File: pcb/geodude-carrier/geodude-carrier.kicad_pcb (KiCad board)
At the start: 2 copper layers, 154.9 x 152.3 mm, 44 parts, among them J1 12V, J2 12V, J3 GND, J30 SCL, J31 SCL, J32 SDA, J33 SDA, J34 3V3, J35 3V3, J36 5V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

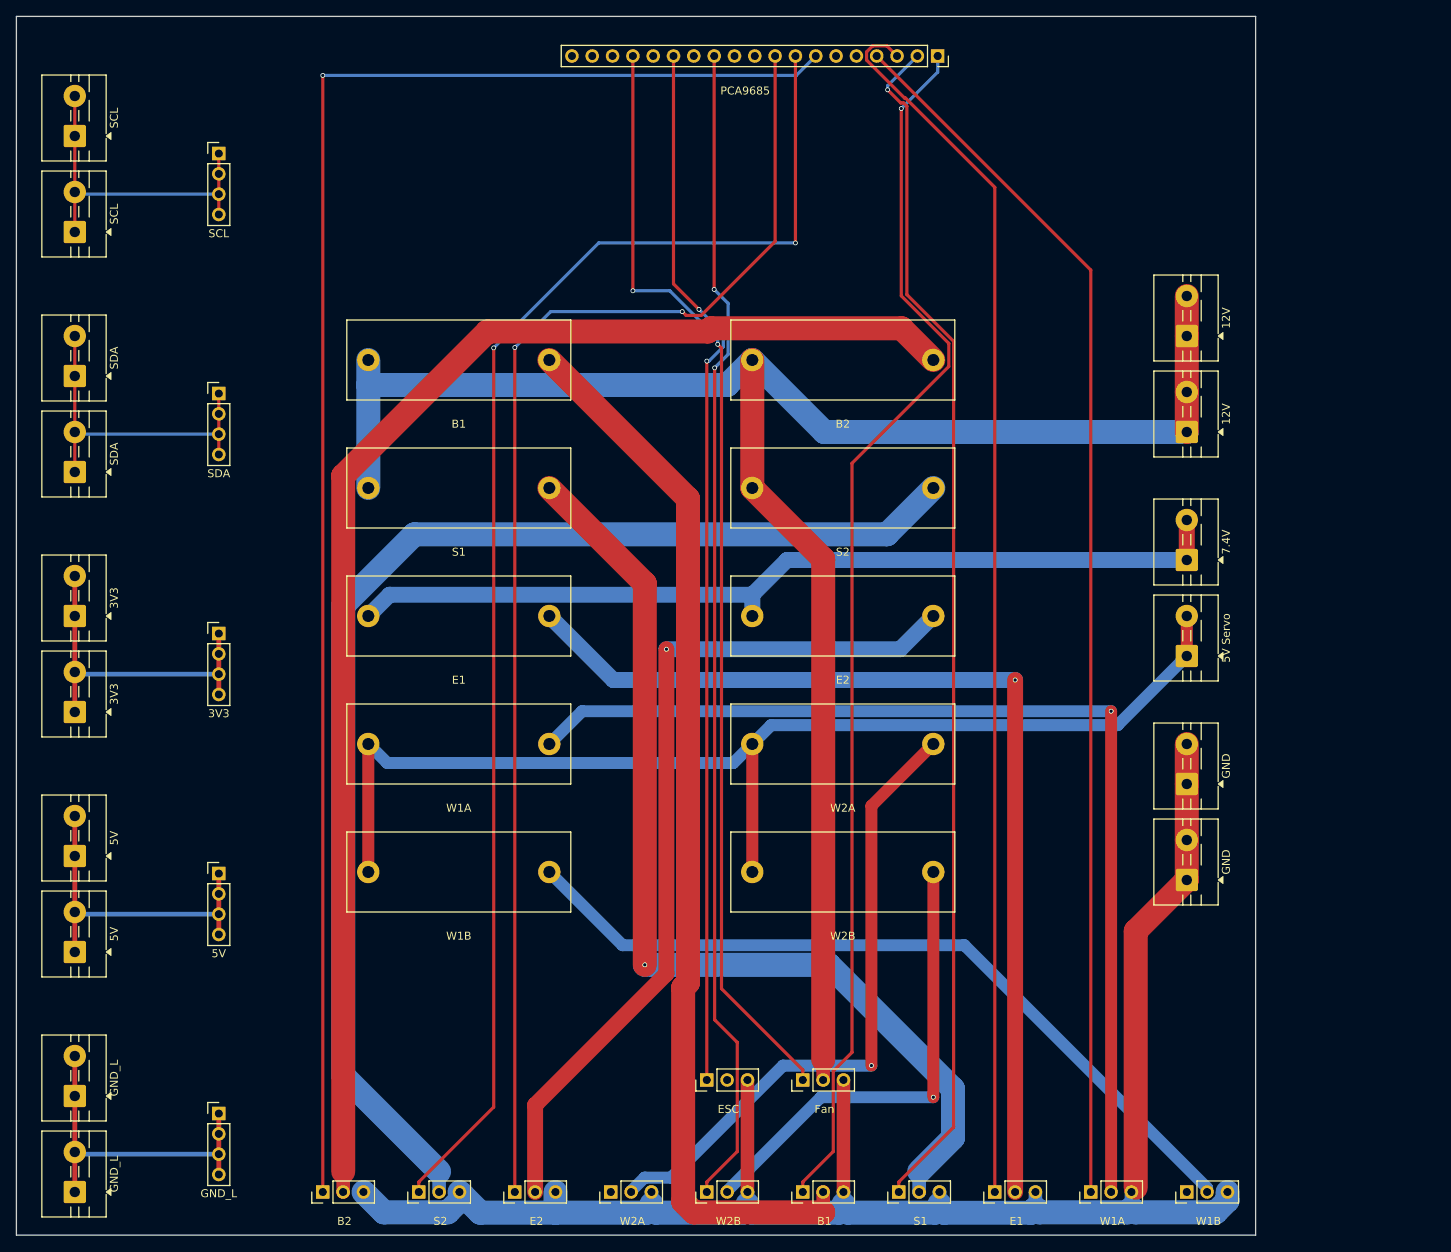
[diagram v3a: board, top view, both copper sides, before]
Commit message: Fully routed: fuses swapped to match servo sides, 0 unconnected, JLCPCB vias
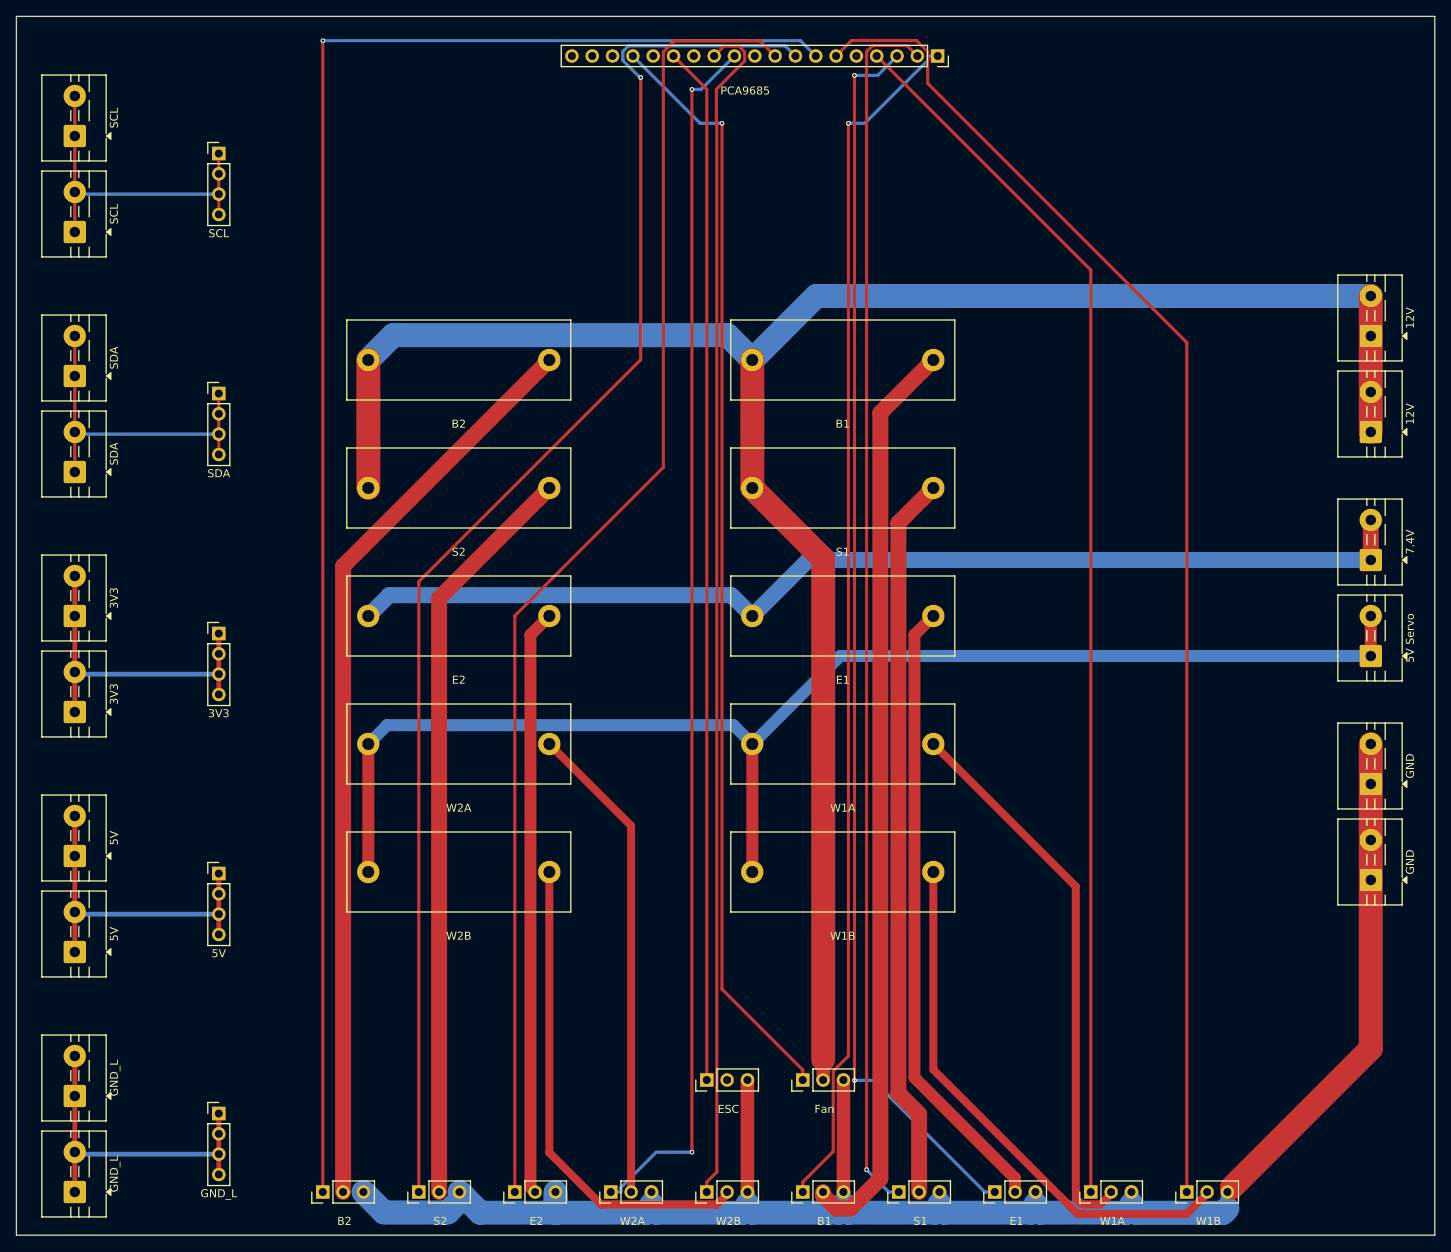
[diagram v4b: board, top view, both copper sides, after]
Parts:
- moved F1 48.0 mm to (106.0, 48.0)
- moved F10 48.0 mm to (58.0, 112.0)
- moved F2 48.0 mm to (106.0, 64.0)
- moved F3 48.0 mm to (106.0, 80.0)
- moved F4 48.0 mm to (106.0, 96.0)
- moved F5 48.0 mm to (106.0, 112.0)
- moved F6 48.0 mm to (58.0, 48.0)
- moved F7 48.0 mm to (58.0, 64.0)
- moved F8 48.0 mm to (58.0, 80.0)
- moved F9 48.0 mm to (58.0, 96.0)
- moved J1 23.0 mm to (172.0, 45.0)
- moved J2 23.0 mm to (172.0, 57.0)
- moved J3 23.0 mm to (172.0, 101.0)
- moved J4 23.0 mm to (172.0, 113.0)
- moved J5 23.0 mm to (172.0, 73.0)
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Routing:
- net PWM_CH4: track 0.00 -> 168.8 mm
- net PWM_CH8: track 0.00 -> 152.4 mm, vias 0 -> 2
- net SV7_PWR: track 158.1 -> 93.7 mm
- net SV4_PWR: track 132.0 -> 69.7 mm, vias 1 -> 0
- net SV6_PWR: track 172.6 -> 114.7 mm
- net SV3_PWR: track 125.5 -> 78.2 mm, vias 1 -> 0
- net SV8_PWR: track 109.7 -> 73.2 mm, vias 1 -> 0
- net SV2_PWR: track 124.1 -> 90.9 mm, vias 1 -> 0
- net SV5_PWR: track 99.1 -> 67.7 mm
- net +12V: track 234.0 -> 257.9 mm
- net +5V_SERVO: track 145.8 -> 168.8 mm
- net +7V4: track 112.9 -> 135.4 mm
- net SV9_PWR: track 80.1 -> 60.2 mm, vias 1 -> 0
- net SV1_PWR: track 133.3 -> 114.9 mm
- net GND: track 217.6 -> 222.8 mm
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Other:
- board size 154.9 x 152.3 mm -> 177.3 x 152.3 mm

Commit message: Production ready: copper pours (GND B.Cu, 12V F.Cu), Gerbers exported, 0 DRC errors
- GND copper pour on back layer (full board)
- +12V copper pour on front layer (right half, power area)
- Gerbers: F.Cu, B.Cu, F.Silk, B.Silk, F.Mask, B.Mask, Edge.Cuts, drill
- DRC: 0 violations, 0 unconnected (3 silk warnings)
- Vias: 0.3mm/0.4mm (JLCPCB free tier)
- Trace widths verified against IPC-2221 at 2oz copper
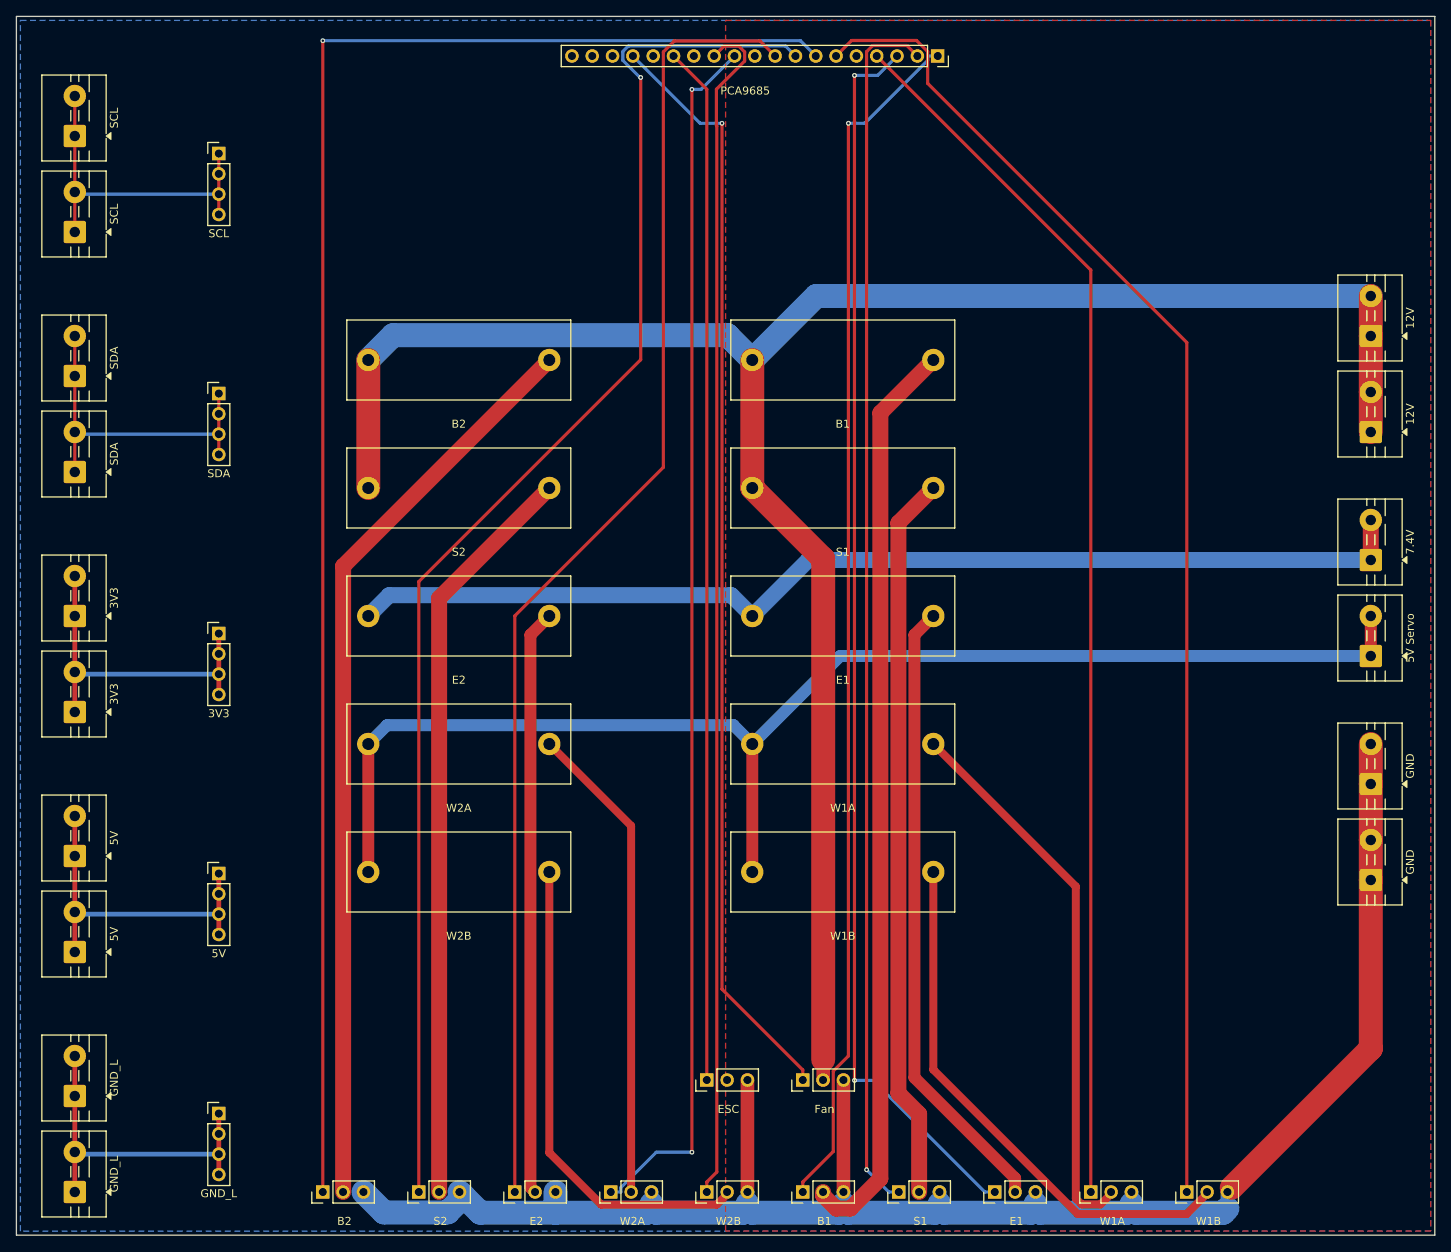
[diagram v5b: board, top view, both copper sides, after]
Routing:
- added copper zone on F.Cu, net +12V
- added copper zone on B.Cu, net GND
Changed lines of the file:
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@@
 		(net "PWM_CH12")
+	)
+	(zone
+		(net "+12V")
+		(layer "F.Cu")
+		(hatch edge 0.5)
+		(connect_pads
+			(clearance 0.5)
+		)
+		(min_thickness 0.3)
+		(fill yes
+			(thermal_gap 0.5)
+			(thermal_bridge_width 0.8)
+			(island_removal_mode 0)
+		)
+		(polygon
+			(pts
+				(xy 91.35 5.55) (xy 179.5 5.55) (xy 179.5 156.893796) (xy 91.35 156.893796)
+			)
+		)
+	)
+	(zone
+		(net "GND")
+		(layer "B.Cu")
+		(hatch edge 0.5)
+		(connect_pads
+			(clearance 0.5)
+		)
+		(min_thickness 0.3)
+		(fill yes
+			(thermal_gap 0.5)
+			(thermal_bridge_width 0.5)
+			(island_removal_mode 0)
+		)
+		(polygon
+			(pts
+				(xy 3.2 5.55) (xy 179.5 5.55) (xy 179.5 156.893796) (xy 3.2 156.893796)
+			)
+		)
 	)
 	(embedded_fonts no)

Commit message: Manual placement adjustments
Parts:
- moved J1 20.4 mm to (151.6, 46.2)
- moved J2 20.4 mm to (151.6, 58.2)
- moved J3 20.4 mm to (151.6, 102.2)
- moved J4 20.4 mm to (151.6, 114.2)
- moved J5 20.4 mm to (151.6, 74.2)
- moved J6 20.4 mm to (151.6, 86.2)
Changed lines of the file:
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@@
 	(footprint "TerminalBlock_MaiXu_MX126-5.0-02P_1x02_P5.00mm"
 		(layer "F.Cu")
-		(at 172 113 90)
+		(at 151.6 114.2 90)
 		(descr "terminal block MaiXu MX126-5.0-02P, 2 pins, pitch 5mm, size 10.5x7.8mm, drill diameter 1.3mm, pad diameter 2.8mm, https://www.lcsc.com/datasheet/lcsc_datasheet_2309150913_MAX-MX126-5-0-03P-GN01-Cu-S-A_C5188435.pdf")
 		(tags "THT terminal block MaiXu MX126-5.0-02P pitch 5mm size 10.5x7.8mm drill 1.3mm pad 2.8mm")
@@
 	(footprint "TerminalBlock_MaiXu_MX126-5.0-02P_1x02_P5.00mm"
 		(layer "F.Cu")
-		(at 172 57 90)
+		(at 151.6 58.2 90)
 		(descr "terminal block MaiXu MX126-5.0-02P, 2 pins, pitch 5mm, size 10.5x7.8mm, drill diameter 1.3mm, pad diameter 2.8mm, https://www.lcsc.com/datasheet/lcsc_datasheet_2309150913_MAX-MX126-5-0-03P-GN01-Cu-S-A_C5188435.pdf")
 		(tags "THT terminal block MaiXu MX126-5.0-02P pitch 5mm size 10.5x7.8mm drill 1.3mm pad 2.8mm")
@@
 	(footprint "TerminalBlock_MaiXu_MX126-5.0-02P_1x02_P5.00mm"
 		(layer "F.Cu")
-		(at 172 45 90)
+		(at 151.6 46.2 90)
 		(descr "terminal block MaiXu MX126-5.0-02P, 2 pins, pitch 5mm, size 10.5x7.8mm, drill diameter 1.3mm, pad diameter 2.8mm, https://www.lcsc.com/datasheet/lcsc_datasheet_2309150913_MAX-MX126-5-0-03P-GN01-Cu-S-A_C5188435.pdf")
 		(tags "THT terminal block MaiXu MX126-5.0-02P pitch 5mm size 10.5x7.8mm drill 1.3mm pad 2.8mm")
@@
 	(footprint "TerminalBlock_MaiXu_MX126-5.0-02P_1x02_P5.00mm"
 		(layer "F.Cu")
-		(at 172 85 90)
+		(at 151.6 86.2 90)
 		(descr "terminal block MaiXu MX126-5.0-02P, 2 pins, pitch 5mm, size 10.5x7.8mm, drill diameter 1.3mm, pad diameter 2.8mm, https://www.lcsc.com/datasheet/lcsc_datasheet_2309150913_MAX-MX126-5-0-03P-GN01-Cu-S-A_C5188435.pdf")
 		(tags "THT terminal block MaiXu MX126-5.0-02P pitch 5mm size 10.5x7.8mm drill 1.3mm pad 2.8mm")
@@
 	(footprint "TerminalBlock_MaiXu_MX126-5.0-02P_1x02_P5.00mm"
 		(layer "F.Cu")
-		(at 172 73 90)
+		(at 151.6 74.2 90)
 		(descr "terminal block MaiXu MX126-5.0-02P, 2 pins, pitch 5mm, size 10.5x7.8mm, drill diameter 1.3mm, pad diameter 2.8mm, https://www.lcsc.com/datasheet/lcsc_datasheet_2309150913_MAX-MX126-5-0-03P-GN01-Cu-S-A_C5188435.pdf")
 		(tags "THT terminal block MaiXu MX126-5.0-02P pitch 5mm size 10.5x7.8mm drill 1.3mm pad 2.8mm")
@@
 	(footprint "TerminalBlock_MaiXu_MX126-5.0-02P_1x02_P5.00mm"
 		(layer "F.Cu")
-		(at 172 101 90)
+		(at 151.6 102.2 90)
 		(descr "terminal block MaiXu MX126-5.0-02P, 2 pins, pitch 5mm, size 10.5x7.8mm, drill diameter 1.3mm, pad diameter 2.8mm, https://www.lcsc.com/datasheet/lcsc_datasheet_2309150913_MAX-MX126-5-0-03P-GN01-Cu-S-A_C5188435.pdf")
 		(tags "THT terminal block MaiXu MX126-5.0-02P pitch 5mm size 10.5x7.8mm drill 1.3mm pad 2.8mm")
